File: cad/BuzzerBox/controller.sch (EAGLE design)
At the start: 76 parts, among them IC1 LM317MBSTT3, Q1 BSS138, Q2 BSS138, U1 MCP23017-E/SO, X1 1751251, X10 1751251, X11 1751248, X2 1751251, X3 1751251, X4 1751251, X5 1751251, X6 1751251, X7 1751251, X8 1751251, X9 1751251

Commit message: PCB V1
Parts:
- removed C3: 10uF, resistor:CPOL-US085CS-1AR
- removed IC1: LM317MBSTT3, v-reg:LM317MBSTT3
- removed X1, X10, X2, X3, X4, X5, X6, X7, X8, X9: 1751251, con-phoenix-350:1751251
- removed X11: 1751248, con-phoenix-350:1751248
- added 12V_IN: 1751248, custom-350:1751248
- added BUZZER0, BUZZER1, BUZZER2, BUZZER3, BUZZER4, BUZZER5, BUZZER6, BUZZER7, BUZZER8, BUZZER9: 1751251, custom-350:1751251
- added D3: 1N4002, diode:1N4004
- added LDO1: LM1084-V, v-reg-2:LM1084-V
- renumbered B1 to PRO_MICRO, SV1 to RPI_GPIO, U1 to MCP23017
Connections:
- new net N$32: 12V_IN-2.K, D3.A
- net +12V: now also D3.C, LDO1.IN; no longer IC1.IN, X11-2.K
- net +5V: now also LDO1.OUT; no longer IC1.OUT
- net GND: now also 12V_IN-1.K, BUZZER0-1.K, BUZZER1-1.K, BUZZER2-1.K, BUZZER3-1.K, BUZZER4-1.K, BUZZER5-1.K, BUZZER6-1.K, BUZZER7-1.K, BUZZER8-1.K, BUZZER9-1.K, LDO1.ADJ; no longer C3.+, C3.-, IC1.ADJ, X1-1.K, X10-1.K, X11-1.K, X2-1.K, X3-1.K, X4-1.K, X5-1.K, X6-1.K, X7-1.K, X8-1.K, X9-1.K
- net N$18: now also BUZZER0-3.K; no longer X10-3.K
- net N$20: now also BUZZER9-3.K; no longer X9-3.K
- net N$23: now also BUZZER4-2.K; no longer X5-2.K
- net N$24: now also BUZZER7-3.K; no longer X8-3.K
- net N$25: now also BUZZER8-3.K; no longer X3-3.K
- net N$26: now also BUZZER1-3.K; no longer X2-3.K
- net N$27: now also BUZZER2-3.K; no longer X1-3.K
- net N$28: now also BUZZER3-3.K; no longer X6-3.K
- net N$29: now also BUZZER4-3.K; no longer X5-3.K
- net N$30: now also BUZZER5-3.K; no longer X4-3.K
- net N$31: now also BUZZER6-3.K; no longer X7-3.K
- net N$35: now also BUZZER5-2.K; no longer X4-2.K
- net N$36: now also BUZZER1-2.K; no longer X2-2.K
- net N$37: now also BUZZER8-2.K; no longer X3-2.K
- net N$38: now also BUZZER7-2.K; no longer X8-2.K
- net N$39: now also BUZZER9-2.K; no longer X9-2.K
- net N$4: now also BUZZER6-2.K; no longer X7-2.K
- net N$40: now also BUZZER0-2.K; no longer X10-2.K
- net N$45: now also BUZZER3-2.K; no longer X6-2.K
- net N$46: now also BUZZER2-2.K; no longer X1-2.K
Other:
- note removed: "C3 helps in ripple rejection upto 15dB"

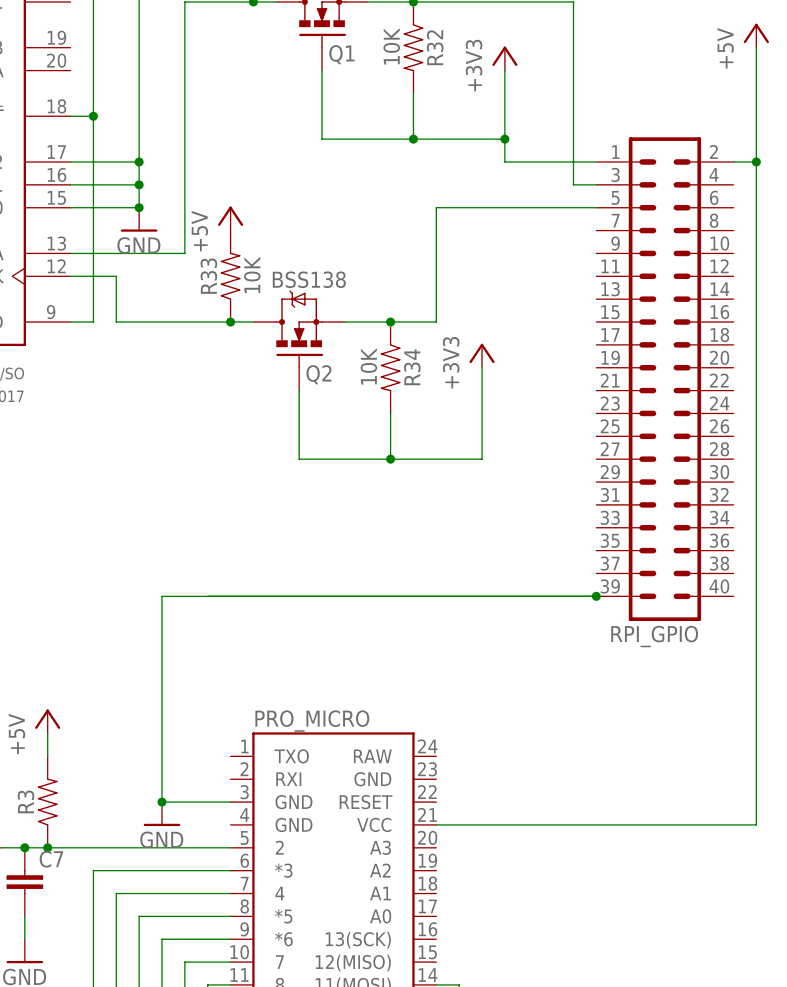
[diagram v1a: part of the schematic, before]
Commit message: Fix obvious pcb issues from V1
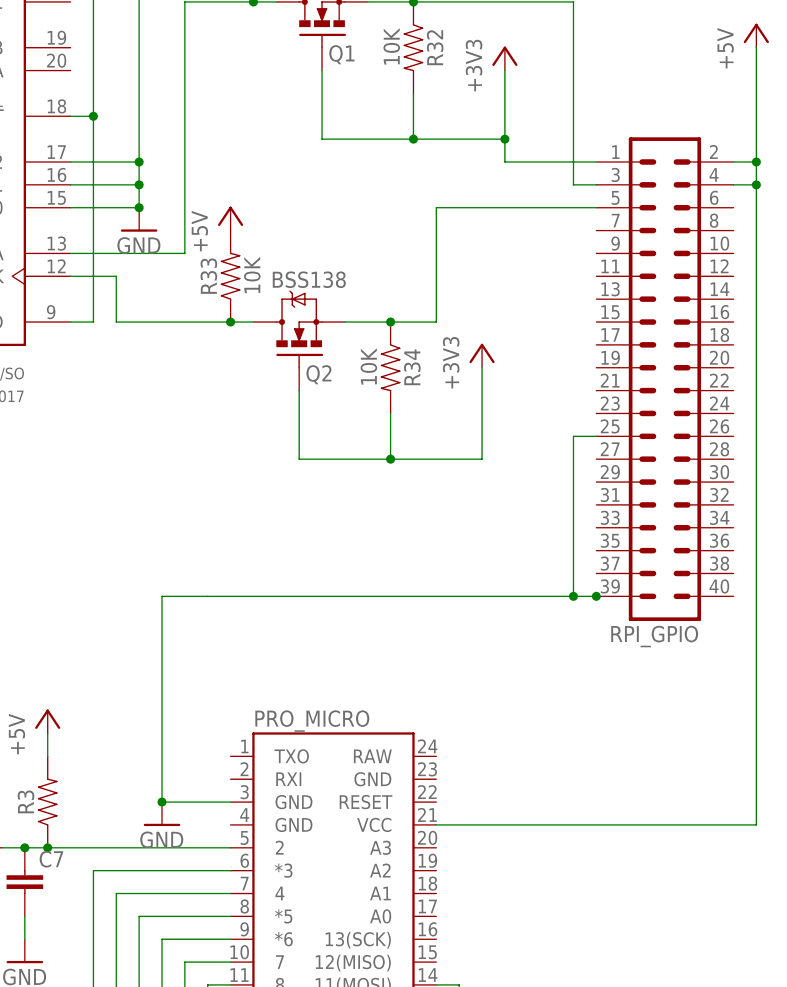
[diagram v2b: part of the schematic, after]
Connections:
- net +5V: now also RPI_GPIO.4
- net GND: now also RPI_GPIO.25
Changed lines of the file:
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@@
 <wire x1="147.32" y1="88.9" x2="139.7" y2="88.9" width="0.1524" layer="91"/>
 <pinref part="RPI_GPIO" gate="G$1" pin="39"/>
-<wire x1="187.96" y1="111.76" x2="144.78" y2="111.76" width="0.1524" layer="91"/>
+<wire x1="185.42" y1="111.76" x2="144.78" y2="111.76" width="0.1524" layer="91"/>
 <wire x1="139.7" y1="88.9" x2="139.7" y2="111.76" width="0.1524" layer="91"/>
-<wire x1="139.7" y1="111.76" x2="187.96" y2="111.76" width="0.1524" layer="91"/>
+<wire x1="139.7" y1="111.76" x2="144.78" y2="111.76" width="0.1524" layer="91"/>
 <junction x="139.7" y="88.9"/>
 <junction x="187.96" y="111.76"/>
+<pinref part="RPI_GPIO" gate="G$1" pin="25"/>
+<wire x1="185.42" y1="111.76" x2="187.96" y2="111.76" width="0.1524" layer="91"/>
+<wire x1="187.96" y1="129.54" x2="185.42" y2="129.54" width="0.1524" layer="91"/>
+<wire x1="185.42" y1="129.54" x2="185.42" y2="111.76" width="0.1524" layer="91"/>
+<junction x="185.42" y="111.76"/>
 </segment>
 <segment>
@@
 <pinref part="PRO_MICRO" gate="G$1" pin="VCC"/>
 <wire x1="205.74" y1="86.36" x2="170.18" y2="86.36" width="0.1524" layer="91"/>
-<wire x1="205.74" y1="160.02" x2="205.74" y2="86.36" width="0.1524" layer="91"/>
-</segment>
-<segment>
+<wire x1="205.74" y1="160.02" x2="205.74" y2="157.48" width="0.1524" layer="91"/>
+<pinref part="RPI_GPIO" gate="G$1" pin="4"/>
+<wire x1="205.74" y1="157.48" x2="205.74" y2="86.36" width="0.1524" layer="91"/>
+<wire x1="203.2" y1="157.48" x2="205.74" y2="157.48" width="0.1524" layer="91"/>
+<junction x="205.74" y="157.48"/>
+</segment>
+<segment>

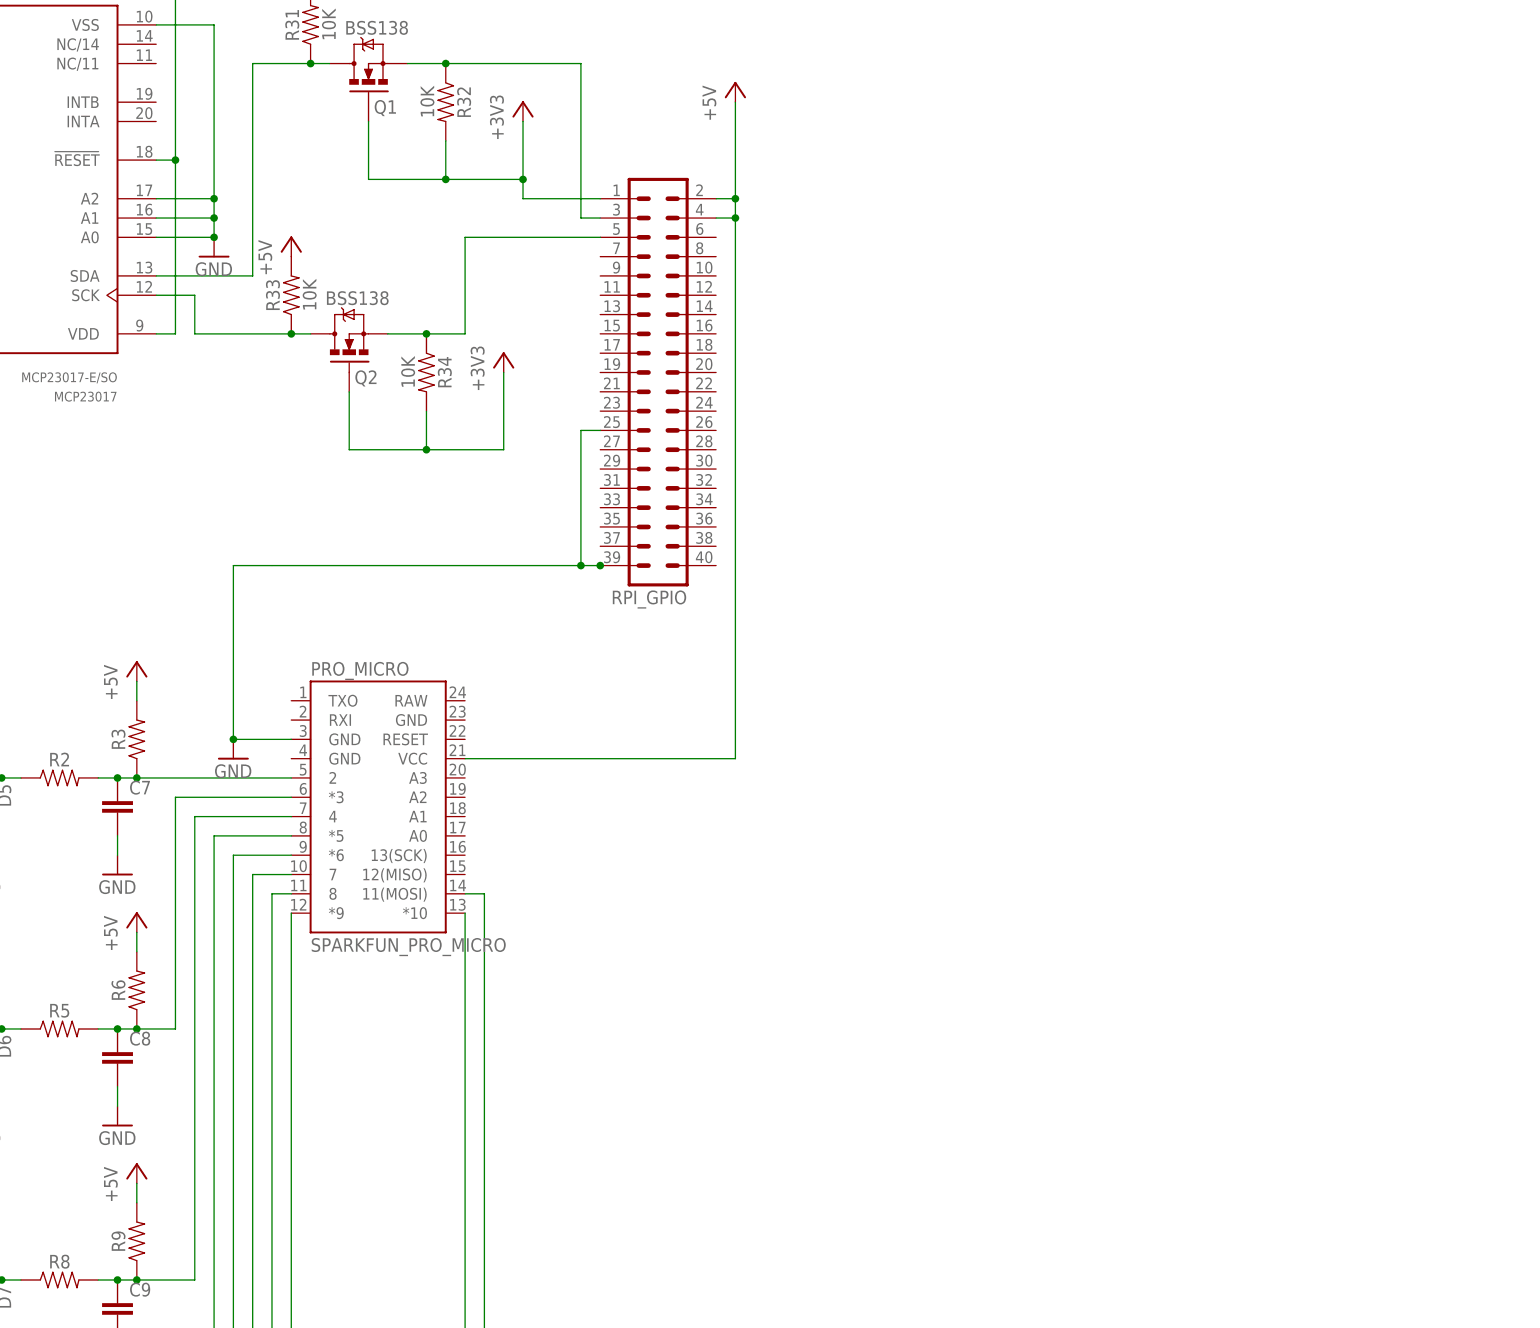
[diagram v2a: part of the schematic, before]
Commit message: Add 7-Segment-Display to Layout
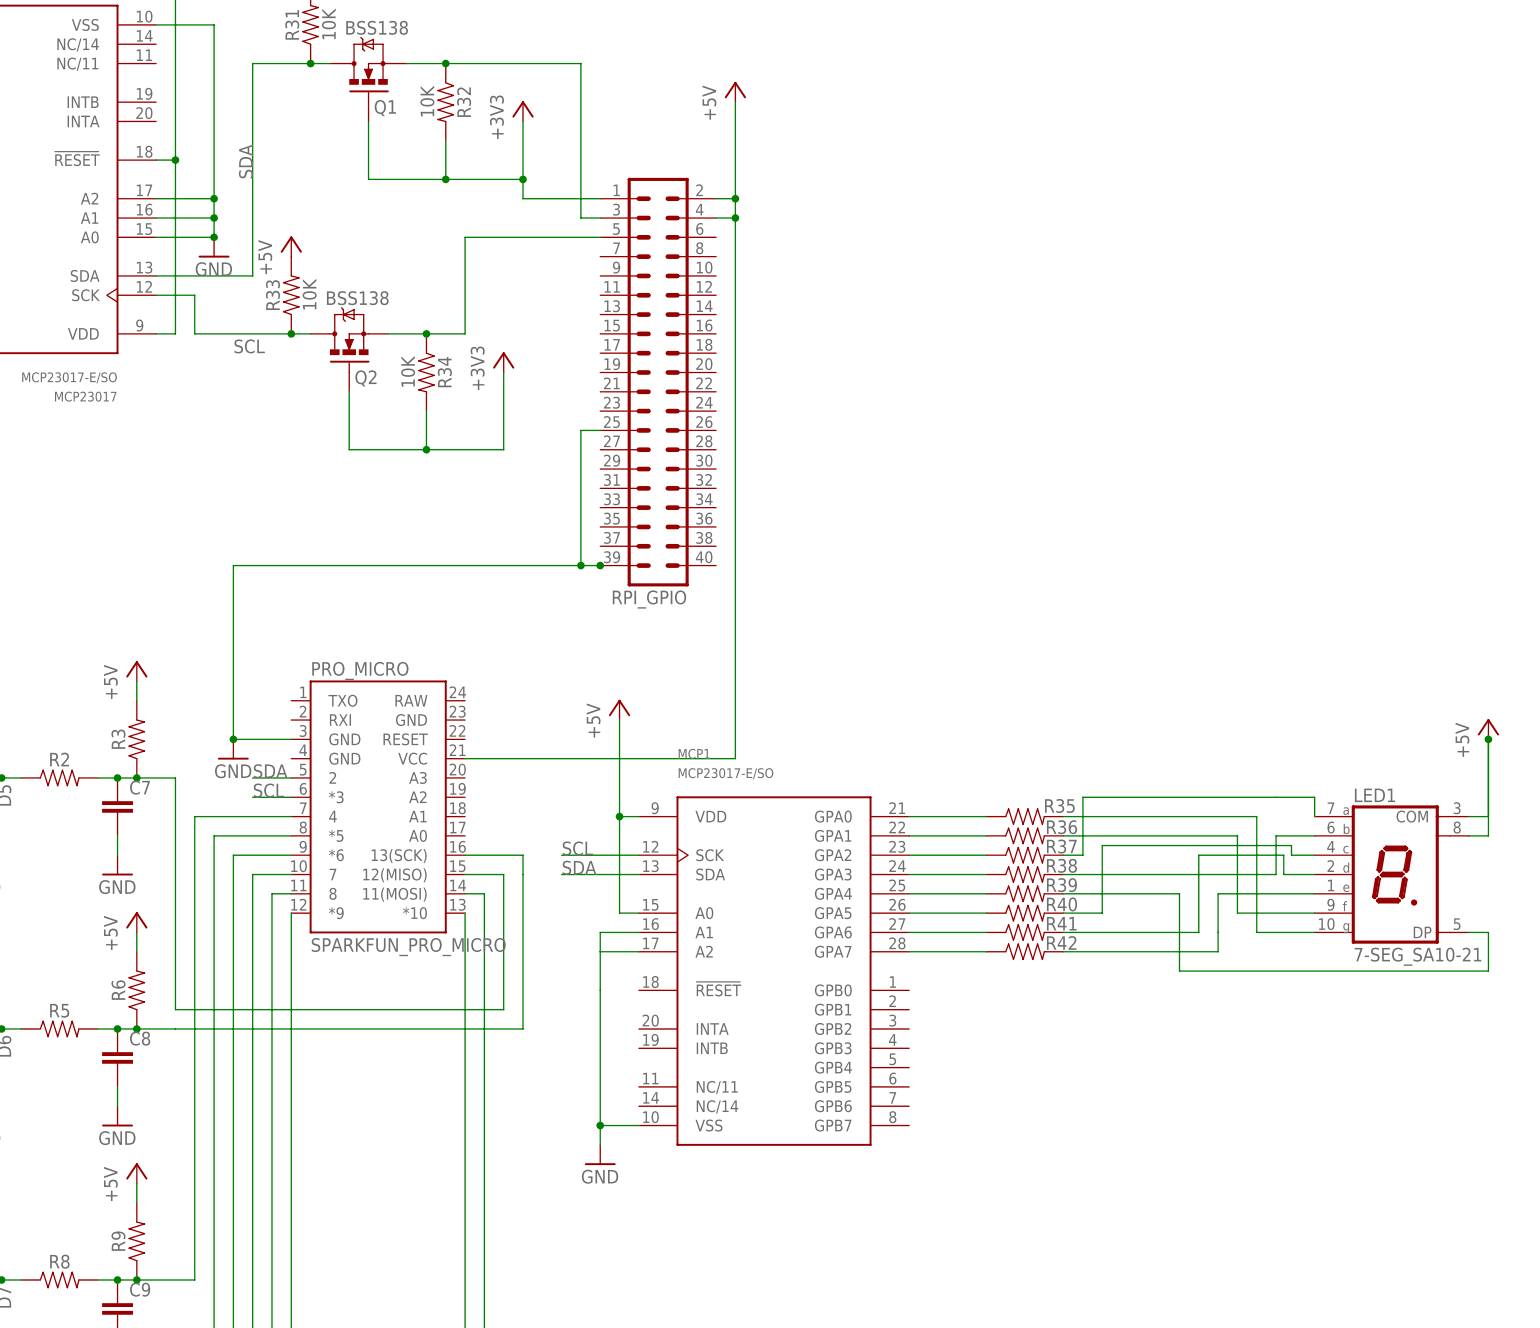
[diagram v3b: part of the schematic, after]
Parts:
- added LED1: 7-SEG_SA10-21, display-kingbright:7-SEG_SA10-21
- added MCP1: MCP23017-E/SO, microchip:MCP23017-E/SO
- added R35, R36, R37, R38, R39, R40, R41, R42: (no value), SparkFun-Resistors:RESISTOR0805
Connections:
- new net N$44: LED1.F, R36.2
- new net N$47: LED1.A, R37.2
- new net N$48: LED1.E, R42.2
- new net N$49: MCP1.GPA7, R42.1
- new net N$51: LED1.D, R41.2
- new net N$52: LED1.C, R40.2
- new net N$53: LED1.DP, R39.2
- new net N$54: MCP1.GPA0, R35.1
- new net N$55: MCP1.GPA1, R36.1
- new net N$56: MCP1.GPA2, R37.1
- new net N$57: MCP1.GPA3, R38.1
- new net N$58: MCP1.GPA4, R39.1
- new net N$59: MCP1.GPA5, R40.1
- new net N$60: MCP1.GPA6, R41.1
- new net SCL: MCP1.SCK, MCP23017.SCK, PRO_MICRO.*3, Q2.D, R33.1
- new net SDA: MCP1.SDA, MCP23017.SDA, PRO_MICRO.2, Q1.D, R31.1
- net +5V: now also LED1.COM@1, LED1.COM@2, MCP1.A0, MCP1.VDD
- net GND: now also MCP1.A1, MCP1.A2, MCP1.VSS
- net N$1: now also PRO_MICRO.12(MISO); no longer PRO_MICRO.2
- net N$33: now also LED1.B, R38.2; no longer MCP23017.SDA, Q1.D, R31.1
- net N$43: now also LED1.G, R35.2; no longer MCP23017.SCK, Q2.D, R33.1
- net N$5: now also PRO_MICRO.13(SCK); no longer PRO_MICRO.*3

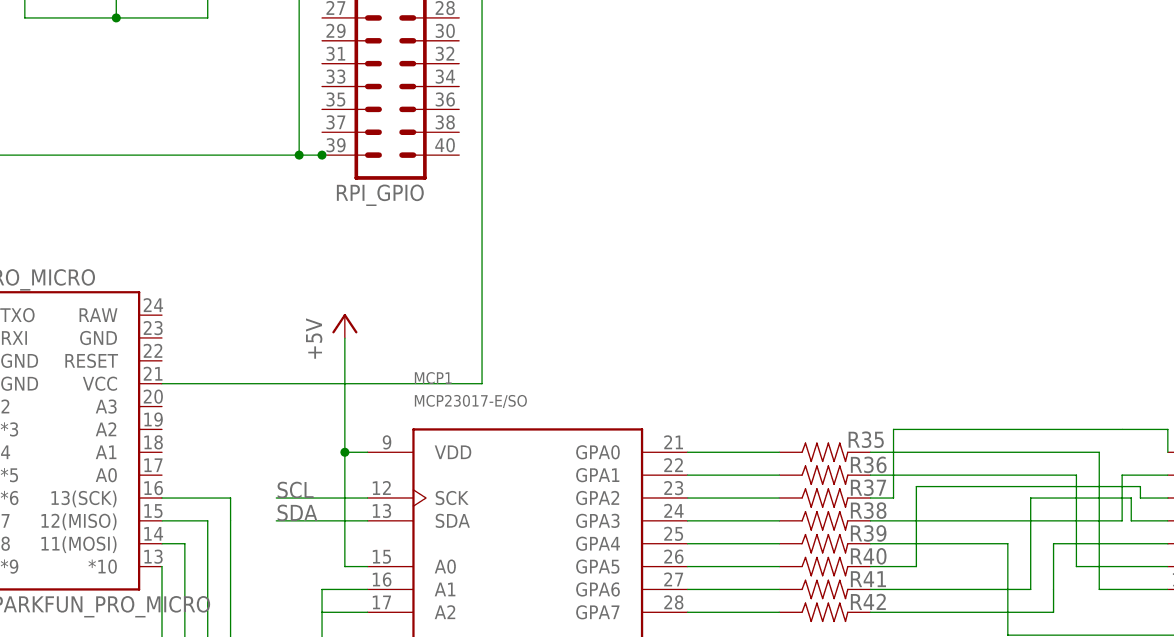
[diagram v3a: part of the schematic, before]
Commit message: Add release button to board
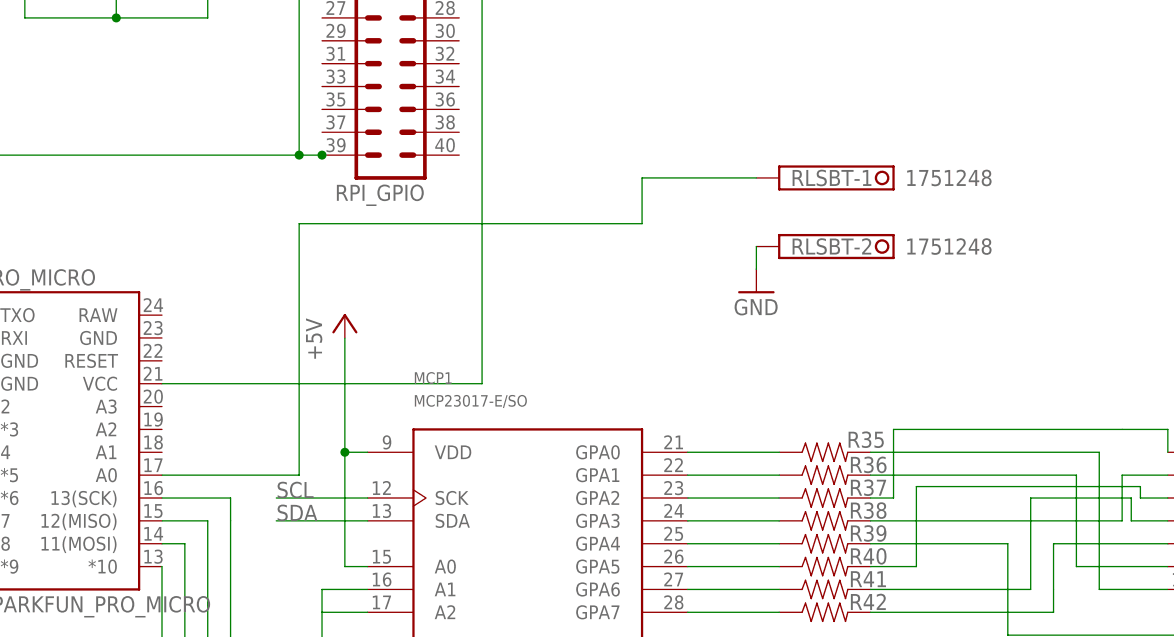
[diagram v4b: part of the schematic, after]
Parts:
- added RLSBT: 1751248, con-phoenix-350:1751248
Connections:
- new net N$50: PRO_MICRO.A0, RLSBT-1.K
- net GND: now also RLSBT-2.K
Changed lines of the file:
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@@
 <part name="GND24" library="supply1" library_urn="urn:adsk.eagle:library:371" deviceset="GND" device=""/>
 <part name="P+7" library="supply1" library_urn="urn:adsk.eagle:library:371" deviceset="+5V" device=""/>
+<part name="RLSBT" library="con-phoenix-350" library_urn="urn:adsk.eagle:library:174" deviceset="1751248" device="" package3d_urn="urn:adsk.eagle:package:9395/1"/>
+<part name="GND25" library="supply1" library_urn="urn:adsk.eagle:library:371" deviceset="GND" device=""/>
 </parts>
 <sheets>
@@
 <instance part="P+7" gate="1" x="190.5" y="93.98" smashed="yes">
 <attribute name="VALUE" x="187.96" y="88.9" size="1.778" layer="96" rot="R90"/>
+</instance>
+<instance part="RLSBT" gate="-1" x="238.76" y="109.22" smashed="yes">
+<attribute name="NAME" x="240.03" y="108.331" size="1.778" layer="95"/>
+<attribute name="VALUE" x="252.73" y="108.331" size="1.778" layer="96"/>
+</instance>
+<instance part="RLSBT" gate="-2" x="238.76" y="101.6" smashed="yes">
+<attribute name="NAME" x="240.03" y="100.711" size="1.778" layer="95"/>
+<attribute name="VALUE" x="252.73" y="100.711" size="1.778" layer="96"/>
+</instance>
+<instance part="GND25" gate="1" x="236.22" y="96.52" smashed="yes">
+<attribute name="VALUE" x="233.68" y="93.98" size="1.778" layer="96"/>
 </instance>
 </instances>
@@
 <wire x1="187.96" y1="63.5" x2="187.96" y2="60.96" width="0.1524" layer="91"/>
 </segment>
+<segment>
+<pinref part="RLSBT" gate="-2" pin="K"/>
+<pinref part="GND25" gate="1" pin="GND"/>
+<wire x1="236.22" y1="101.6" x2="236.22" y2="99.06" width="0.1524" layer="91"/>
+</segment>
 </net>
 <net name="+3V3" class="0">
@@
 </segment>
 </net>
+<net name="N$50" class="0">
+<segment>
+<pinref part="PRO_MICRO" gate="G$1" pin="A0"/>
+<wire x1="170.18" y1="76.2" x2="185.42" y2="76.2" width="0.1524" layer="91"/>
+<wire x1="185.42" y1="76.2" x2="185.42" y2="104.14" width="0.1524" layer="91"/>
+<wire x1="185.42" y1="104.14" x2="223.52" y2="104.14" width="0.1524" layer="91"/>
+<wire x1="223.52" y1="104.14" x2="223.52" y2="109.22" width="0.1524" layer="91"/>
+<pinref part="RLSBT" gate="-1" pin="K"/>
+<wire x1="223.52" y1="109.22" x2="236.22" y2="109.22" width="0.1524" layer="91"/>
+</segment>
+</net>
